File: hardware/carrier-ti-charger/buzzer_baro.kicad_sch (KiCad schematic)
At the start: 21 parts, among them J12 CONTROLS, SW2 K3-1280S-F1, SW3 K3-1280S-F1, U10 BMP581, U13 TCA9534PWR, U9 SN74LVC1G17DBVR

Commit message: TI charger
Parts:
- C28, C29, C30, C40: value 100n -> 100n 50V
- R27, R48, R49, R50, R51, R52, R53, R54, R55: value 100k -> 100k 1%
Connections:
- net CTRL_P7 renamed SW_ON_N
- net SW_ON_N: no longer J12.6 (Pin_6)
- no-connect marks 3 -> 4
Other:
- note added: "MUTE"
- note added: "Physical controls"
- note added: "Pull-ups, all expander inputs high when open"
- note added: "Wi-Fi"
- moved on the sheet: BZ1, C28, C29, C30, C40, J12, R27, R28, R48, R49, R50, R51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

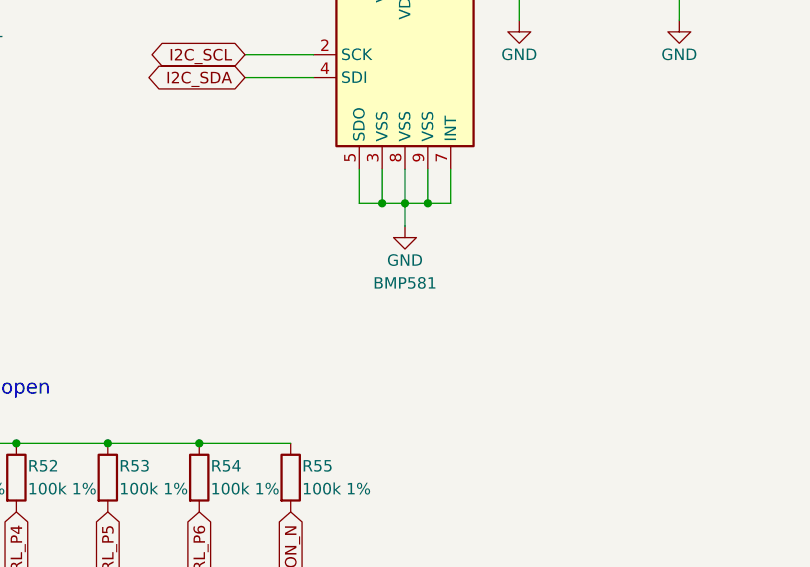
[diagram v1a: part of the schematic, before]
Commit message: Switch parts (BMP580, TPS259474L) due to stock shortage.
Also, add overvoltage (OVLO) protection.
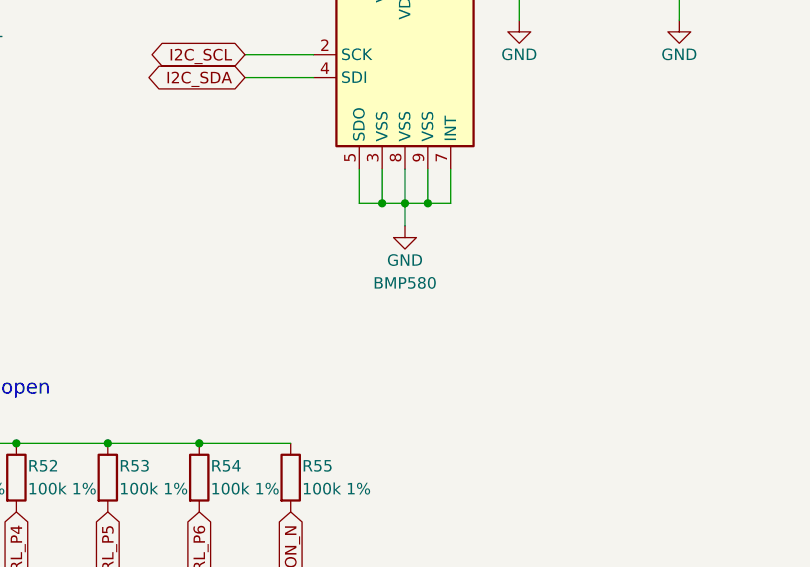
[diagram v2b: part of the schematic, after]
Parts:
- U10: value BMP581 -> BMP580; LCSC C5362283 -> C22391138; MPN BMP581 -> BMP580
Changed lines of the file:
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@@
 			)
 		)
-		(property "Value" "BMP581"
+		(property "Value" "BMP580"
 			(at 190.5 91.44 0)
 			(show_name no)
@@
 			)
 		)
-		(property "Datasheet" "https://www.lcsc.com/datasheet/C5362283.pdf"
+		(property "Datasheet" "https://www.lcsc.com/datasheet/C22391138.pdf"
 			(at 190.5 66.04 0)
 			(hide yes)
@@
 			)
 		)
-		(property "LCSC" "C5362283"
+		(property "LCSC" "C22391138"
 			(at 190.5 66.04 0)
 			(hide yes)
@@
 			)
 		)
-		(property "MPN" "BMP581"
+		(property "MPN" "BMP580"
 			(at 190.5 66.04 0)
 			(hide yes)

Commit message: Other MH's.
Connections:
- net ESP_3V3 renamed +ESP_3V3
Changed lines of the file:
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@@
 	)
 	(symbol
-		(lib_id "carrier:ESP_3V3")
+		(lib_id "carrier:+ESP_3V3")
 		(at 175.26 48.26 0)
 		(unit 1)
@@
 			)
 		)
-		(property "Value" "ESP_3V3"
+		(property "Value" "+ESP_3V3"
 			(at 175.26 44.45 0)
 			(show_name no)
@@
 			)
 		)
-		(property "Description" "Power symbol creates a global label with name \"ESP_3V3\""
+		(property "Description" "Power symbol creates a global label with name \"+ESP_3V3\""
 			(at 175.26 48.26 0)
 			(hide yes)
@@
 	)
 	(symbol
-		(lib_id "carrier:ESP_3V3")
+		(lib_id "carrier:+ESP_3V3")
 		(at 71.12 40.64 0)
 		(unit 1)
@@
 			)
 		)
-		(property "Value" "ESP_3V3"
+		(property "Value" "+ESP_3V3"
 			(at 71.12 36.83 0)
 			(show_name no)
@@
 			)
 		)
-		(property "Description" "Power symbol creates a global label with name \"ESP_3V3\""
+		(property "Description" "Power symbol creates a global label with name \"+ESP_3V3\""
 			(at 71.12 40.64 0)
 			(hide yes)
@@
 	)
 	(symbol
-		(lib_id "carrier:ESP_3V3")
+		(lib_id "carrier:+ESP_3V3")
 		(at 101.6 109.22 0)
 		(unit 1)
@@
 			)
 		)
-		(property "Value" "ESP_3V3"
+		(property "Value" "+ESP_3V3"
 			(at 101.6 105.41 0)
 			(show_name no)
@@
 			)
 		)
-		(property "Description" "Power symbol creates a global label with name \"ESP_3V3\""
+		(property "Description" "Power symbol creates a global label with name \"+ESP_3V3\""
 			(at 101.6 109.22 0)
 			(hide yes)
@@
 	)
 	(symbol
-		(lib_id "carrier:ESP_3V3")
+		(lib_id "carrier:+ESP_3V3")
 		(at 60.96 106.68 0)
 		(unit 1)
@@
 			)
 		)
-		(property "Value" "ESP_3V3"
+		(property "Value" "+ESP_3V3"
 			(at 60.96 102.87 0)
 			(show_name no)
@@
 			)
 		)
-		(property "Description" "Power symbol creates a global label with name \"ESP_3V3\""
+		(property "Description" "Power symbol creates a global label with name \"+ESP_3V3\""
 			(at 60.96 106.68 0)
 			(hide yes)

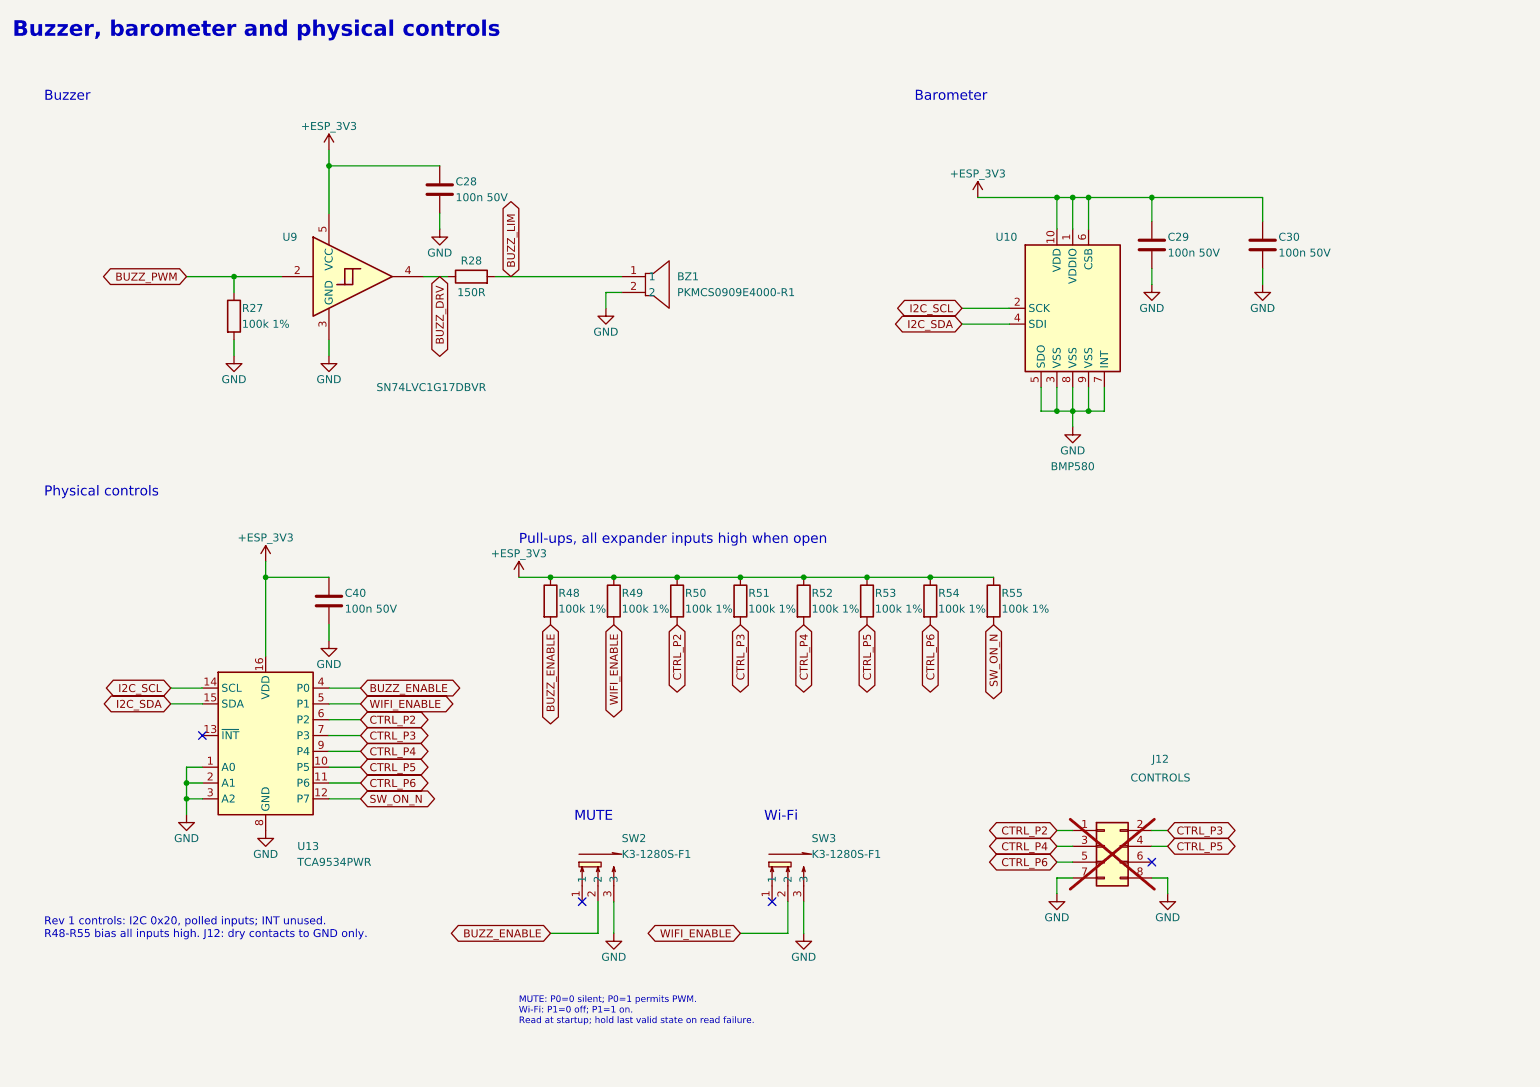
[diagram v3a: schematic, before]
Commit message: Add USB current detection.
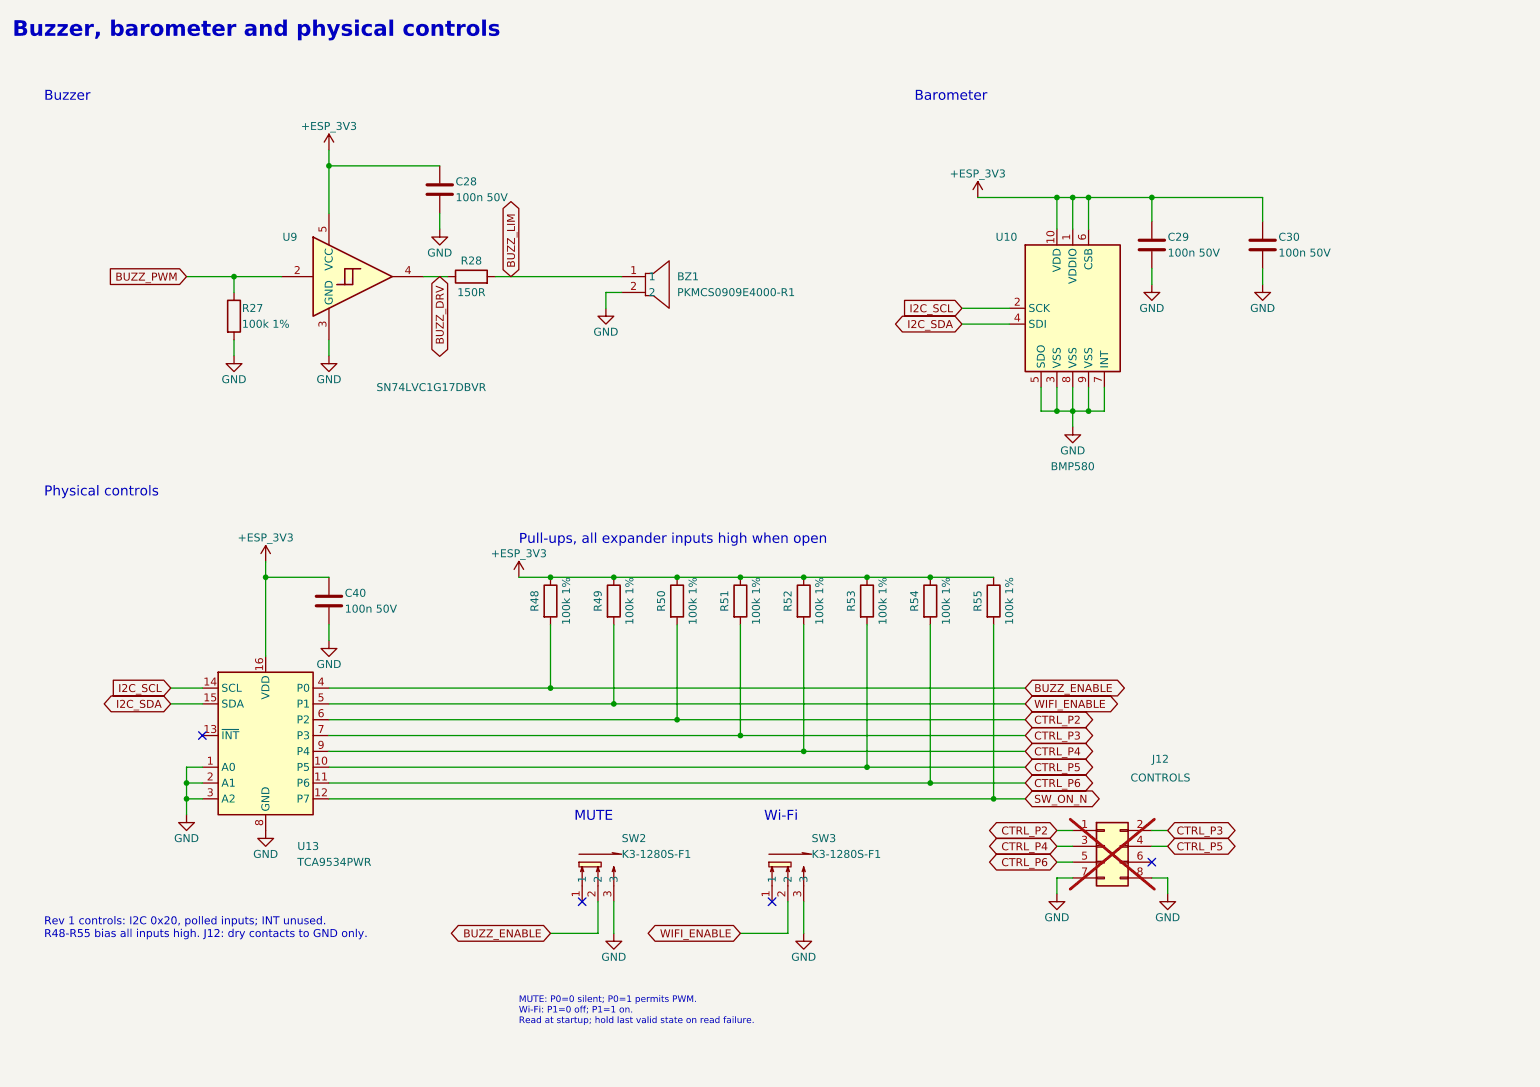
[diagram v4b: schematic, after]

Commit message: Refine resistors.
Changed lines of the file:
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@@
 	)
 	(global_label "BUZZ_ENABLE"
-		(shape bidirectional)
+		(shape input)
 		(at 182.88 127 0)
 		(fields_autoplaced yes)
@@
 		)
 		(property "Intersheetrefs" "${INTERSHEET_REFS}"
-			(at 182.88 127 0)
+			(at 198.8675 127 0)
 			(hide yes)
 			(show_name no)
@@
 	)
 	(global_label "WIFI_ENABLE"
-		(shape bidirectional)
+		(shape input)
 		(at 182.88 129.54 0)
 		(fields_autoplaced yes)
@@
 		)
 		(property "Intersheetrefs" "${INTERSHEET_REFS}"
-			(at 182.88 129.54 0)
-			(hide yes)
-			(show_name no)
+			(at 197.5976 129.54 0)
+			(hide yes)
+			(show_name no)

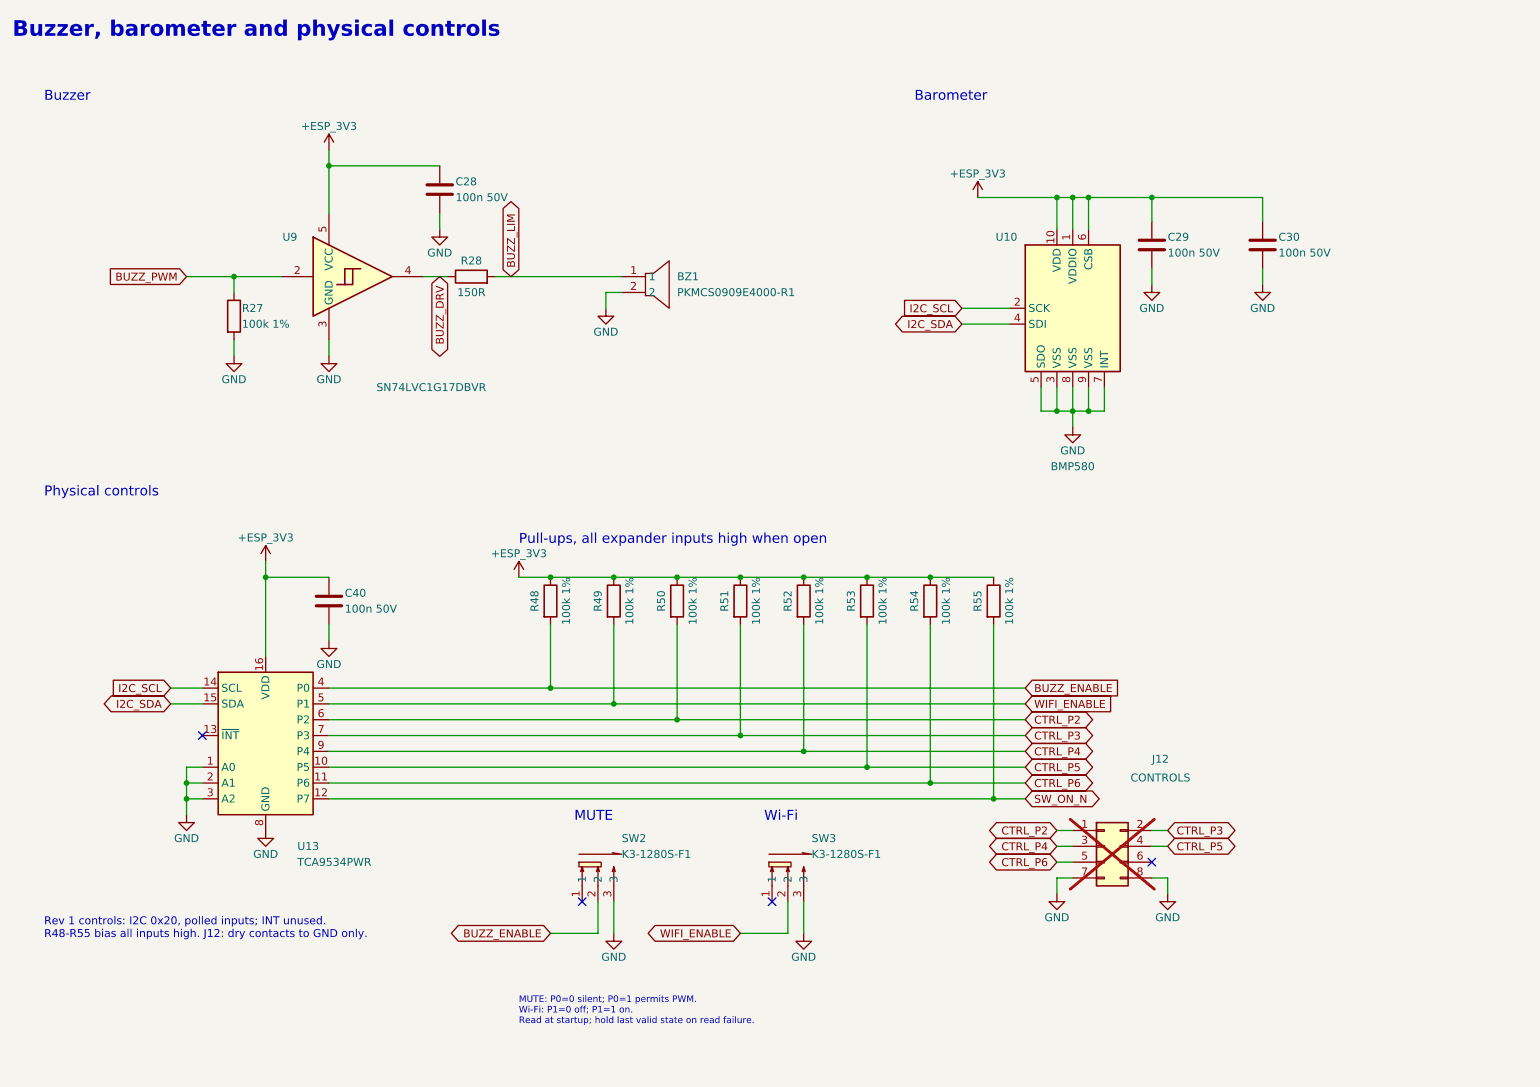
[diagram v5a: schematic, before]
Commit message: Switch to Max M10 on-board chip instead of module.
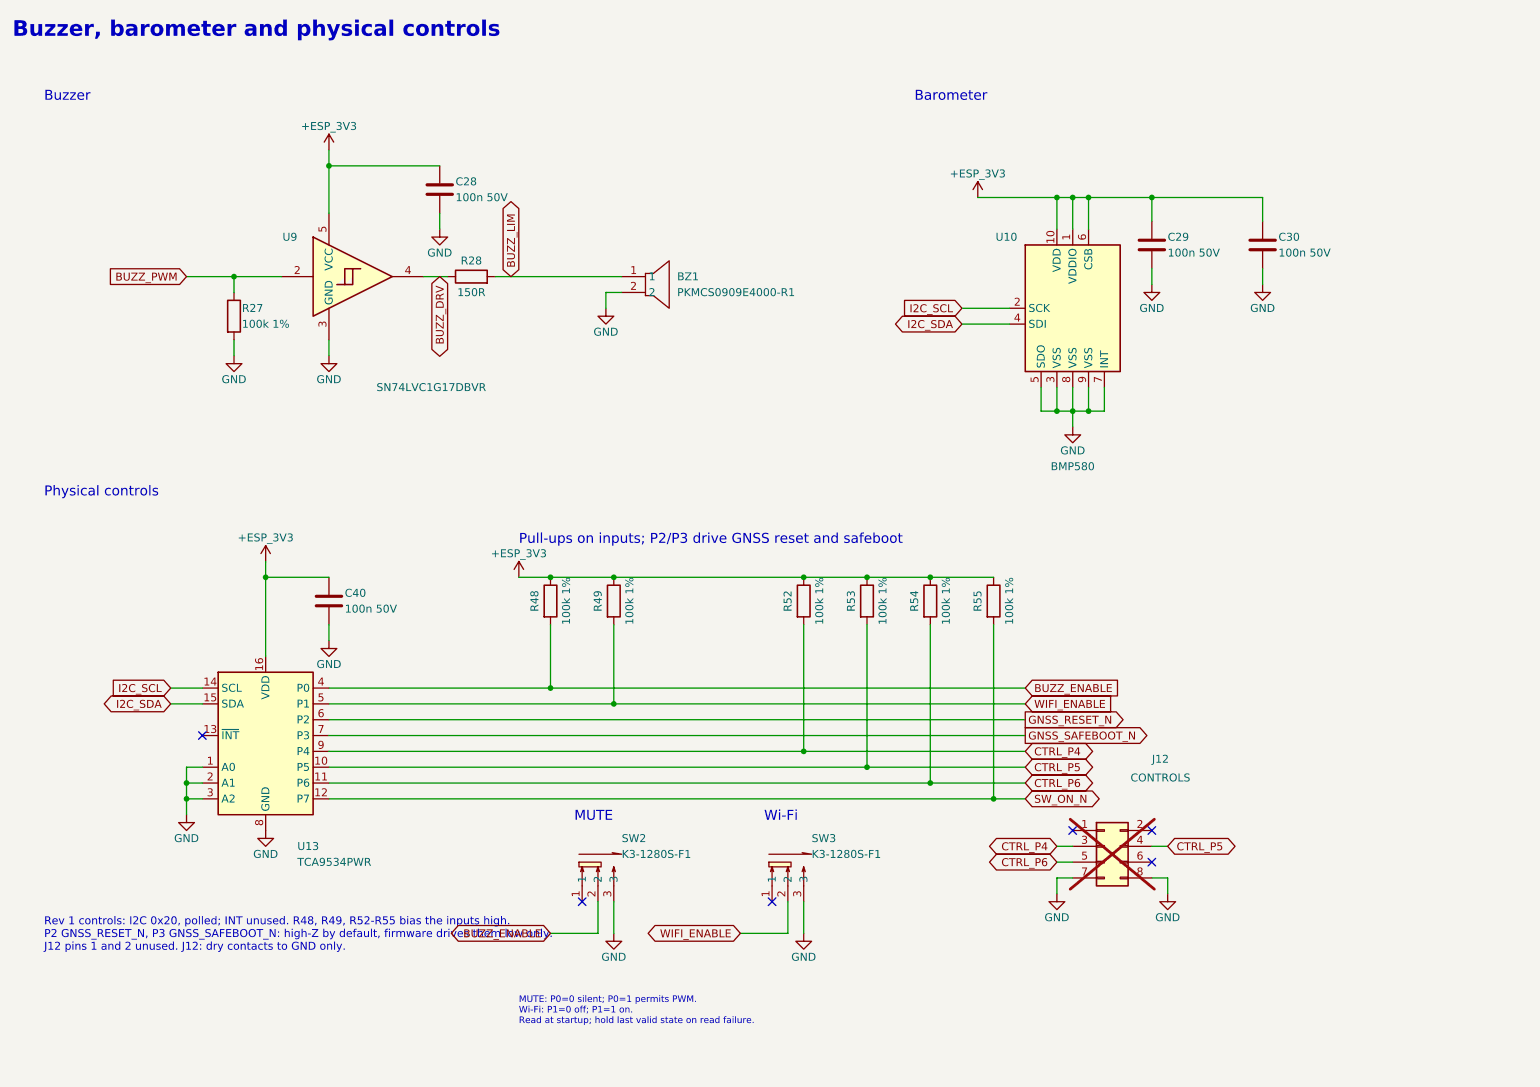
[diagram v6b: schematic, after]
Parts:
- removed R50, R51: 100k 1%, Resistor_SMD:R_0603_1608Metric, symbol Device:R
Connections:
- net CTRL_P2: no longer names the net of J12.1 (Pin_1)
- net CTRL_P2: no longer U13.6 (P2)
- net CTRL_P3: no longer names the net of J12.2 (Pin_2)
- net CTRL_P3: no longer U13.7 (P3)
- new net GNSS_RESET_N: U13.6 (P2)
- new net GNSS_SAFEBOOT_N: U13.7 (P3)
- no-connect marks 4 -> 6
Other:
- note added: "Pull-ups on inputs; P2/P3 drive GNSS reset and safeboot"
- note added: "Rev 1 controls: I2C 0x20, polled; INT unused. R48, R49, R52-R55 bias the inputs high. P2 GNSS_RESET_N, P3 GNSS_SAFEBOOT_N: high-Z by default, firmware drives them low only. J12 pins 1 and 2 unused. J12: dry contacts to GND only."
- note removed: "Pull-ups, all expander inputs high when open"
- note removed: "Rev 1 controls: I2C 0x20, polled inputs; INT unused. R48-R55 bias all inputs high. J12: dry contacts to GND only."

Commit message: Consolidate bom.
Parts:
- C28, C29, C30, C40: value 100n 50V -> 100n 16V; footprint Capacitor_SMD:C_0603_1608Metric -> carrier:C_0402_1005Metric_NoSilk; LCSC C14663 -> C1525; MPN (none) -> CL05B104KO5NNNC
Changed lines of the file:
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@@
 			)
 		)
-		(property "Value" "100n 50V"
+		(property "Value" "100n 16V"
 			(at 223.52 57.15 0)
 			(show_name no)
@@
 			)
 		)
-		(property "Footprint" "Capacitor_SMD:C_0603_1608Metric"
+		(property "Footprint" "carrier:C_0402_1005Metric_NoSilk"
 			(at 220.98 55.88 0)
 			(hide yes)
@@
 			)
 		)
-		(property "LCSC" "C14663"
+		(property "LCSC" "C1525"
+			(at 220.98 55.88 0)
+			(hide yes)
+			(show_name no)
+			(do_not_autoplace no)
+			(effects
+				(font
+					(size 1.27 1.27)
+				)
+			)
+		)
+		(property "MPN" "CL05B104KO5NNNC"
 			(at 220.98 55.88 0)
 			(hide yes)
@@
 			)
 		)
-		(property "Value" "100n 50V"
+		(property "Value" "100n 16V"
 			(at 205.74 57.15 0)
 			(show_name no)
@@
 			)
 		)
-		(property "Footprint" "Capacitor_SMD:C_0603_1608Metric"
+		(property "Footprint" "carrier:C_0402_1005Metric_NoSilk"
 			(at 203.2 55.88 0)
 			(hide yes)
@@
 			)
 		)
-		(property "LCSC" "C14663"
+		(property "LCSC" "C1525"
+			(at 203.2 55.88 0)
+			(hide yes)
+			(show_name no)
+			(do_not_autoplace no)
+			(effects
+				(font
+					(size 1.27 1.27)
+				)
+			)
+		)
+		(property "MPN" "CL05B104KO5NNNC"
 			(at 203.2 55.88 0)
 			(hide yes)
@@
 			)
 		)
-		(property "Value" "100n 50V"
+		(property "Value" "100n 16V"
 			(at 91.44 48.26 0)
 			(show_name no)
@@
 			)
 		)
-		(property "Footprint" "Capacitor_SMD:C_0603_1608Metric"
+		(property "Footprint" "carrier:C_0402_1005Metric_NoSilk"
 			(at 88.9 46.99 0)
 			(hide yes)
@@
 			)
 		)
-		(property "LCSC" "C14663"
+		(property "LCSC" "C1525"
+			(at 88.9 46.99 0)
+			(hide yes)
+			(show_name no)
+			(do_not_autoplace no)
+			(effects
+				(font
+					(size 1.27 1.27)
+				)
+			)
+		)
+		(property "MPN" "CL05B104KO5NNNC"
 			(at 88.9 46.99 0)
 			(hide yes)
@@
 			)
 		)
-		(property "Value" "100n 50V"
+		(property "Value" "100n 16V"
 			(at 73.66 114.3 0)
 			(show_name no)
@@
 			)
 		)
-		(property "Footprint" "Capacitor_SMD:C_0603_1608Metric"
+		(property "Footprint" "carrier:C_0402_1005Metric_NoSilk"
 			(at 71.12 113.03 0)
 			(hide yes)
@@
 			)
 		)
-		(property "LCSC" "C14663"
+		(property "LCSC" "C1525"
 			(at 71.12 113.03 0)
 			(hide yes)
+			(show_name no)
+			(do_not_autoplace no)
+			(effects
+				(font
+					(size 1.27 1.27)
+				)
+			)
+		)
+		(property "MPN" "CL05B104KO5NNNC"
+			(at 71.12 113.03 0)
+			(hide yes)
